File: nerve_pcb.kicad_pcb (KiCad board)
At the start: 6 copper layers, 50 x 50 mm, 85 parts, among them J1 TC2050-IDC, J2 2171750001, J4 472192001, J5 BF030-16A-B1-0360-0277-0600-LB, J6 BF080-20-A-1-L-C, J7 UART, J8 CAN1, J9 CAN2, SW1 SPST, SW2 SPST, U1 ld39150dt33-r, U2 STM32F446RET, U3 TXB0104QPWRQ1, U4 BNO085, U5 BMP390, U6 TJA1051T/3, U7 TJA1051T/3, Y1 8M, Y2 32k768, Y3 32k768

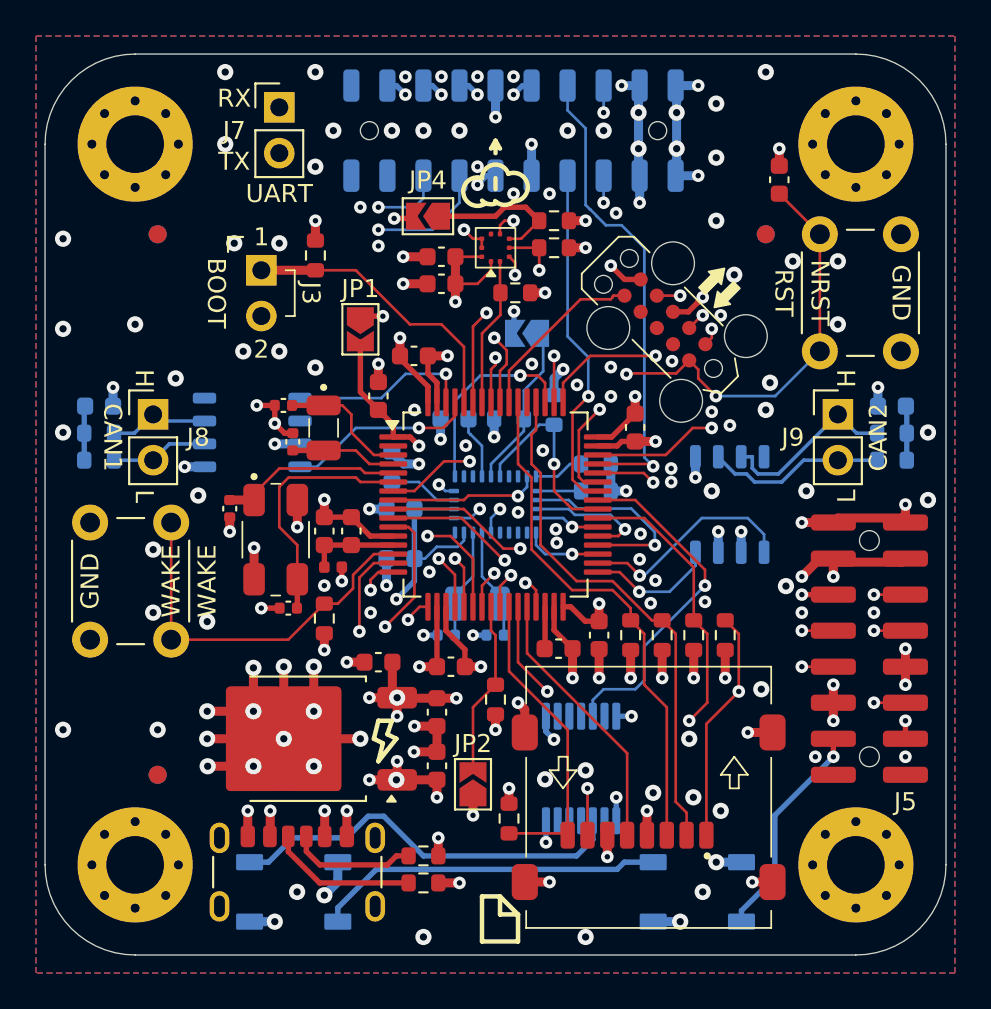
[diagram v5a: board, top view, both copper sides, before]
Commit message: Update for KiCad 9.0 and component library
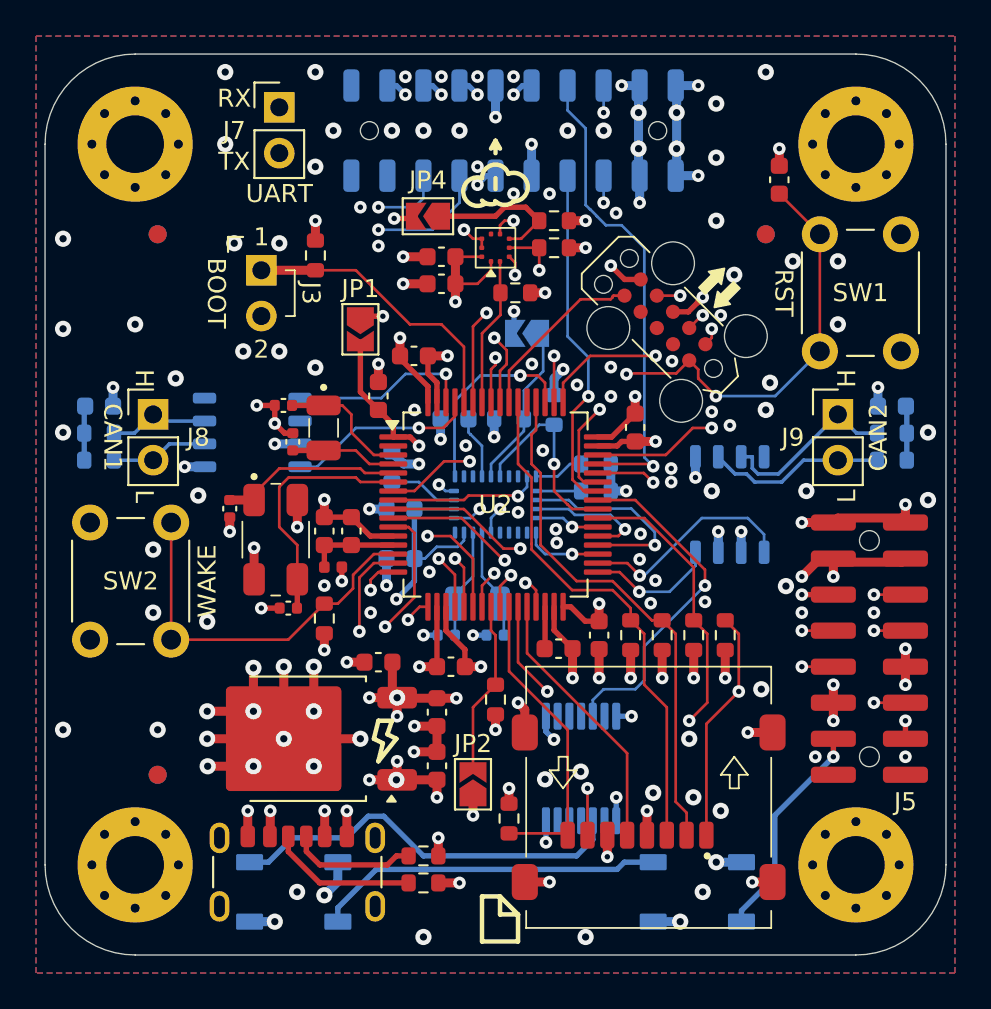
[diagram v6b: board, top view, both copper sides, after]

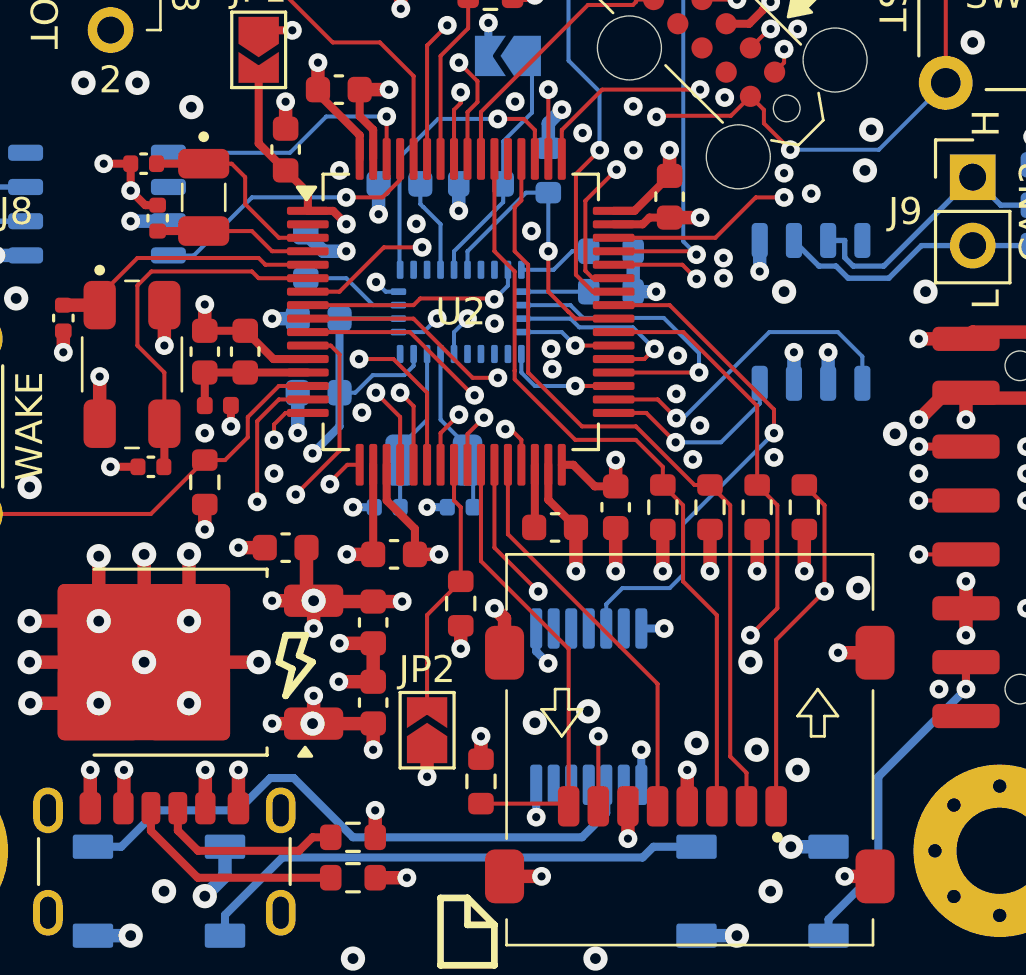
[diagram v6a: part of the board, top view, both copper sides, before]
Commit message: Add minor decoupling caps
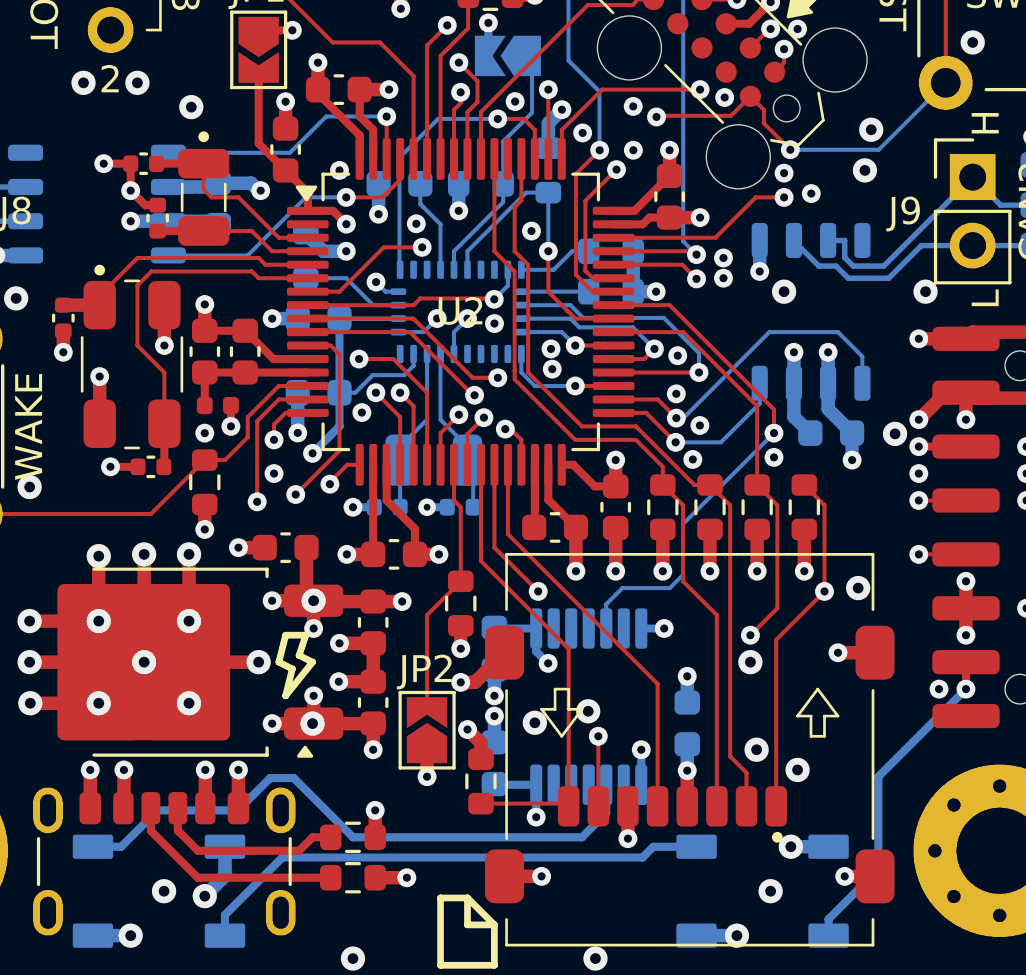
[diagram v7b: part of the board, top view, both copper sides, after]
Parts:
- added C12: 100n, Capacitor_SMD:C_0603_1608Metric, B.Cu at (156.9, 120.3)
- added C15: 100n, Capacitor_SMD:C_0603_1608Metric, B.Cu at (149.8, 117.5)
- added C16: 100n, Capacitor_SMD:C_0603_1608Metric, B.Cu at (149.8, 121.8)
- added C27: 100n, Capacitor_SMD:C_0603_1608Metric, B.Cu at (139.5, 101.0)
- added C28: 100n, Capacitor_SMD:C_0603_1608Metric, B.Cu at (162.2, 109.5)
- renumbered C12 to C13, C13 to C14, C14 to C17, C15 to C18, C16 to C19, C17 to C20, C18 to C21, C19 to C22, C20 to C23, C21 to C24, C22 to C25, C23 to C26, C24 to C29, C25 to C30
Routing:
- net GND: track 108.3 -> 118.3 mm, vias 157 -> 161
- net +5V: track 30.3 -> 35.9 mm
- net +3V3: track 87.1 -> 90.1 mm
